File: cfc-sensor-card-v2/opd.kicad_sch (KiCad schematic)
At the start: 73 parts, among them Q1 DMP2240UDM, Q2 PMV45EN, Q3 DMP3050LVT-7, Q4 DMP3050LVT-7, Q5 PMV45EN, U2 MAX7310, U3 MIC842LYC5, U4 MIC842LYC5, U5 MAX4211FETE

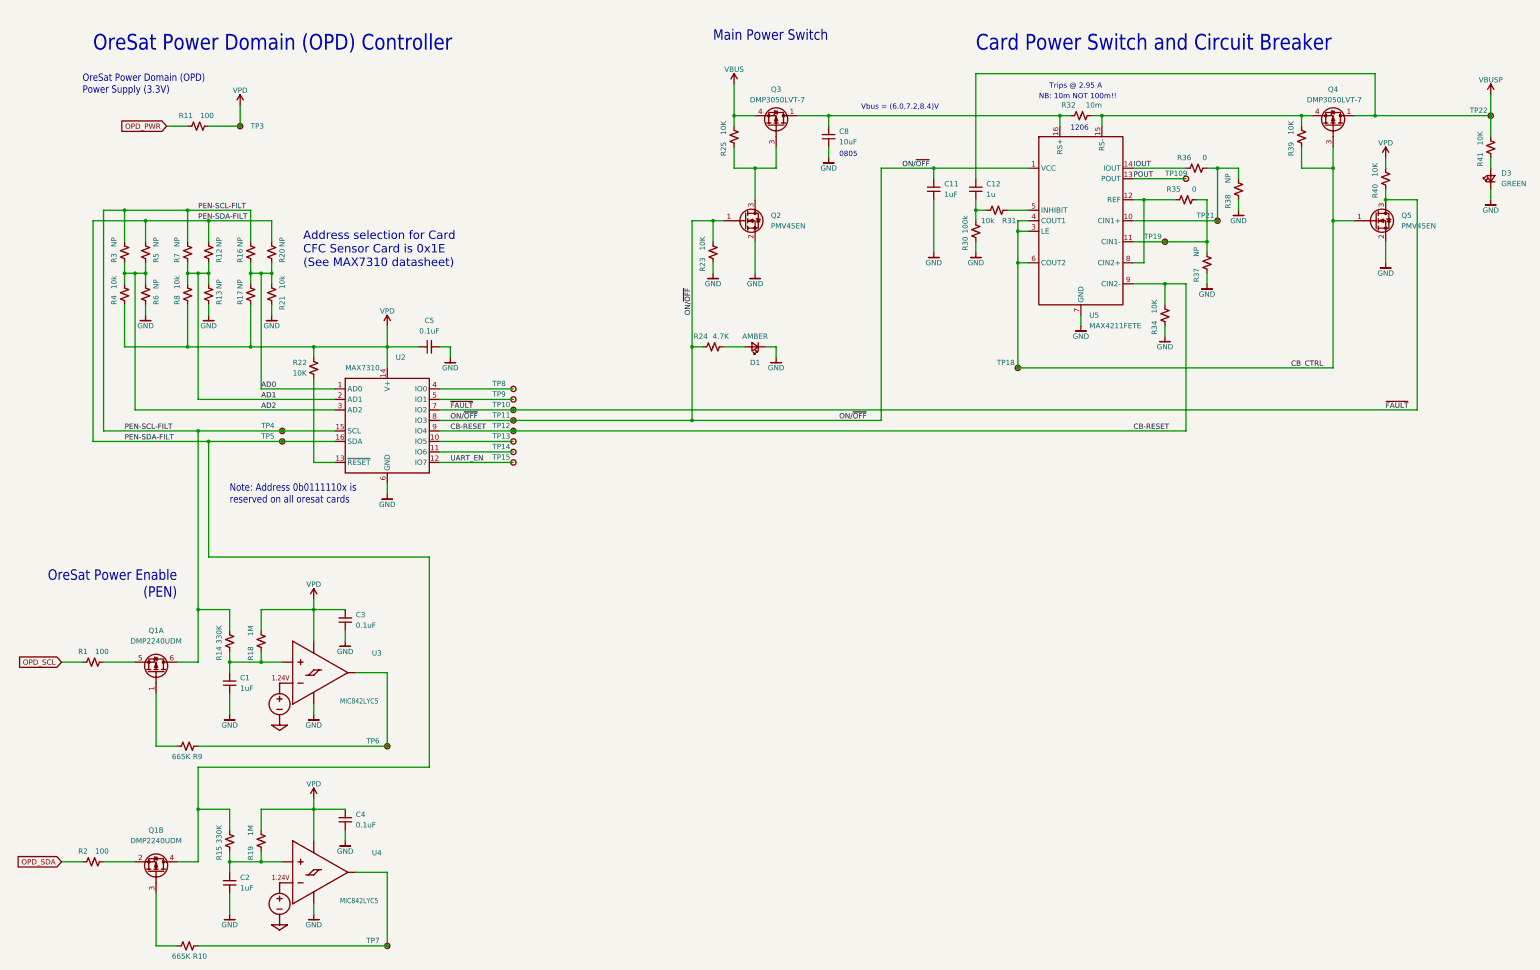
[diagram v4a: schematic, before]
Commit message: Big sweep through to clean up from v2.0 to v2.1 board. Cleaned up all of the Github issues, and even added a MPS2410A CC driver to run the TEC for increased efficiency. Left old switch on board just in case. Lots of cleanup, added some documentation, added pin holes for 1.5 mm alignment pins, now version 2.1
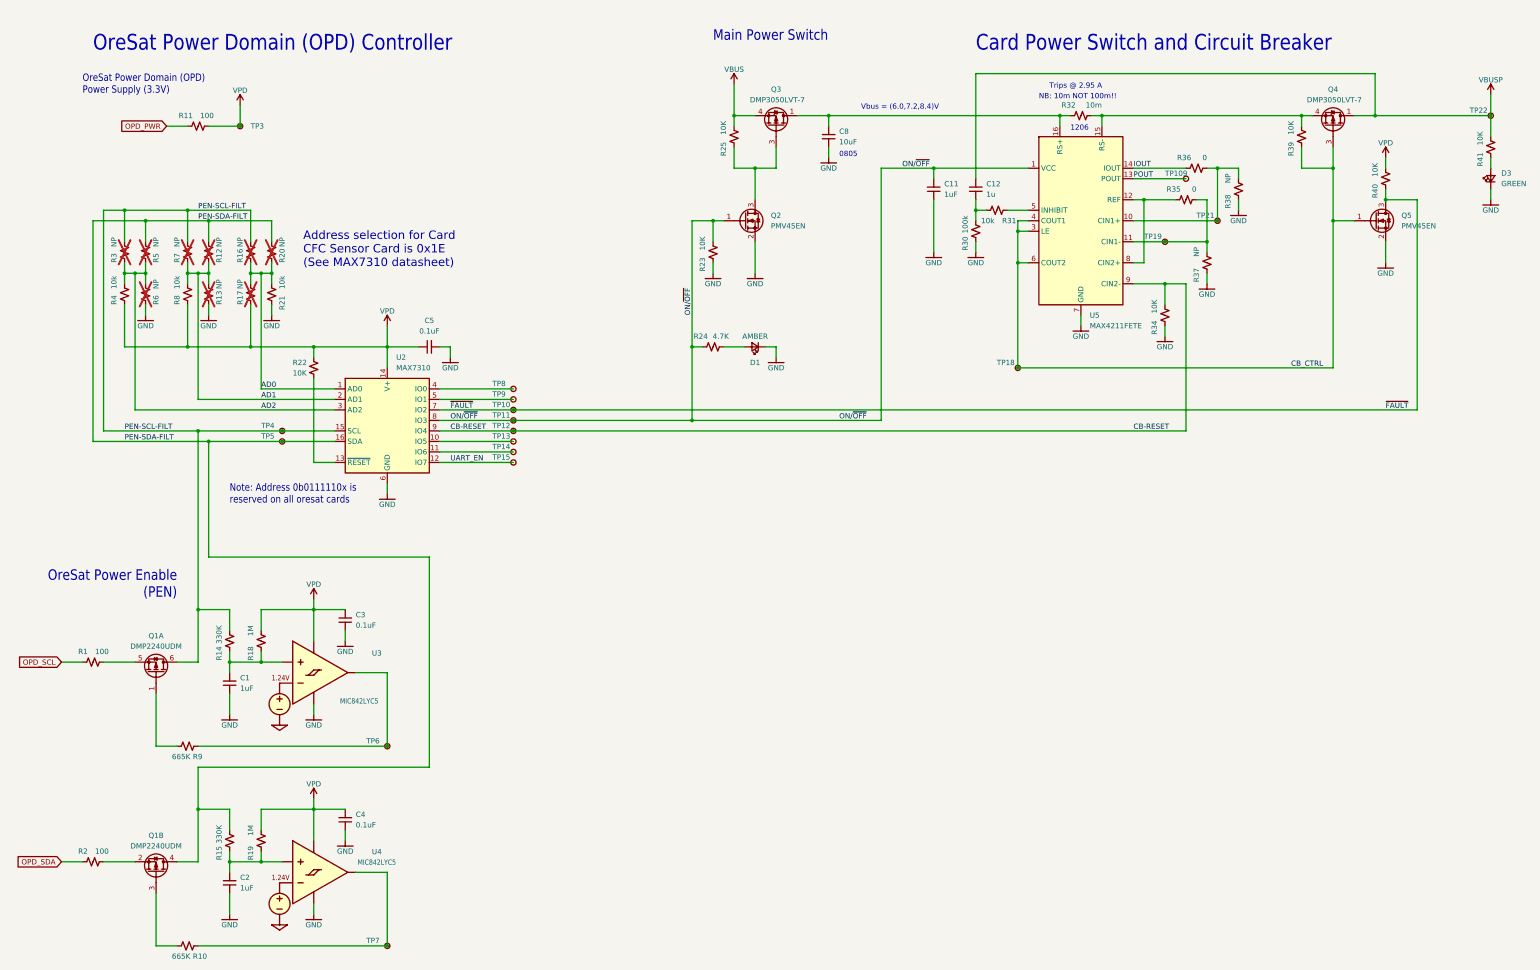
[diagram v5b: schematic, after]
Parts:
- D1, D3: footprint LED_SMD:LED_0603_1608Metric_Pad1.05x0.95mm_HandSolder -> LED_SMD:LED_0603_1608Metric
- Q1: symbol Device:Q_Dual_PMOS_G1S2G2D2S1D1 -> Transistor_FET:Q_Dual_PMOS_G1S2G2D2S1D1
- Q2, Q5: symbol Device:Q_NMOS_GSD -> Transistor_FET:Q_NMOS_GSD
- Q3, Q4: footprint Package_TO_SOT_SMD:SOT-23-6_Handsoldering -> Package_TO_SOT_SMD:TSOT-23-6
- R12, R13, R16, R17, R20, R3, R5, R6, R7: now not fitted
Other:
- company: (none) -> Portland State Aerospace Society
- title: (none) -> CFC Sensor Card
